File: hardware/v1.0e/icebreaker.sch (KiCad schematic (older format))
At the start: 133 parts, among them J1 Jumper, J10 Jumper, J11 Jumper, J12 Jumper, J13 Jumper, J14 Jumper, J15 Jumper, J16 Jumper, J17 Jumper, J18 Jumper, J19 Jumper, J2 Jumper, J20 Flash, J21 PMOD, J22 PMOD, J23 PMOD, J24 PMOD, J25 RGB Led, J26 5V AUX, J27 5V AUX, J28 CRESET, J29 Jumper, J3 Jumper, J30 Jumper, J31 RGB Led, J32 WS2812, J33 RGB Led, J34 SADD, J4 Jumper, J5 Jumper, J6 Jumper, J7 Jumper, J8 Jumper, J9 Jumper, P1 pkl_USB_OTG, P2 UP, P3 UP, P4 UP, P5 UP, P6 RAM_CS, Q1 BSS138, SW1 TACT, SW2 TACT, SW3 TACT, SW4 TACT, U1 93C46B-SOT-23-6, U2 3.3V, U3 1V2, U4 FT2232H, U5 W25Q, U6 ICE5LP4K-SG48, U7 12MHz

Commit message: Corrected the RGB pin numbering.
The original symbol was based on the older ice5lp not ice40up. The
numbering/naming of those pins changed. Now it should be fixed.

Fixes #31 and #32
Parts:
- U6: value ICE5LP4K-SG48 -> ICE40UP5K-SG48; symbol pkl_lattice:ICE5LP4K-SG48 -> pkl_lattice:ICE40UP5K-SG48
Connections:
- net EB_OD0: now also J33.2 (Pin_2), J34.2 (Pin_2), R28.1; no longer J33.4 (Pin_4)
- net EB_OD2: now also J33.4 (Pin_4); no longer J33.2 (Pin_2), J34.2 (Pin_2), R28.1
- net ET_OD0: now also J31.2 (Pin_2), Q1.1 (G), R7.2; no longer J31.4 (Pin_4)
- net ET_OD2: now also J31.4 (Pin_4); no longer J31.2 (Pin_2), Q1.1 (G), R7.2
- net ~LED_RGB0: now also D11.1 (RK), J25.2 (Pin_2), U6.39 (RGB0); no longer D11.3 (BK), J25.4 (Pin_4), U6.41 (RGB0)
- net ~LED_RGB2: now also D11.3 (BK), J25.4 (Pin_4), U6.41 (RGB2); no longer D11.1 (RK), J25.2 (Pin_2), U6.39 (RGB2)
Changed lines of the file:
@@
 Title "iCEBreaker"
 Date ""
-Rev "V1.0d"
+Rev "V1.0e"
 Comp "1BitSquared"
 Comment1 "2019 (C) 1BitSquared <info@1bitsquared.com>"
@@
 $EndDescr
 $Comp
-L pkl_lattice:ICE5LP4K-SG48 U6
+L pkl_lattice:ICE40UP5K-SG48 U6
 U 1 1 5A512943
 P 9600 4200
 F 0 "U6" H 9600 6370 50  0000 C CNN
-F 1 "ICE5LP4K-SG48" H 9600 6277 50  0000 C CNN
+F 1 "ICE40UP5K-SG48" H 9600 6277 50  0000 C CNN
 F 2 "pkl_housings_dfn_qfn:QFN-48-1EP_7x7mm_Pitch0.5mm" H 11900 4400 50  0001 C CNN
 F 3 "" H 11900 4400 50  0001 C CNN
@@
 	10600 4100 10800 4100
 Text Label 10800 4100 0    50   ~ 0
-~LED_RGB0
+~LED_RGB2
 Text Label 10800 4000 0    50   ~ 0
 ~LED_RGB1
 Text Label 10800 3900 0    50   ~ 0
-~LED_RGB2
+~LED_RGB0
 Text Notes 600  1700 0    100  ~ 0
 FTDI Programmer/UART/FIFO
@@
 ~LED_RGB1
 Text Label 15600 8600 0    50   ~ 0
-~LED_RGB2
-Text Label 15600 8700 0    50   ~ 0
 ~LED_RGB0
+Text Label 15600 8700 0    50   ~ 0
+~LED_RGB2
 Wire Wire Line
 	13300 4400 13500 4400
@@
 	15150 9700 15250 9700
 Text Label 15250 9300 0    50   ~ 0
-~LED_RGB2
+~LED_RGB0
 Text Label 15250 9500 0    50   ~ 0
 ~LED_RGB1
 Text Label 15250 9700 0    50   ~ 0
-~LED_RGB0
+~LED_RGB2
 $Comp
 L pkl_misc:pkl_double_jumper_ncno J30
@@
 	7400 10400 7300 10400
 Text Label 8000 10400 0    50   ~ 0
-ET_OD2
-Text Label 7300 10400 2    50   ~ 0
-ET_OD1
-Text Label 8000 10500 0    50   ~ 0
 ET_OD0
+Text Label 8000 10500 0    50   ~ 0
+ET_OD2
 Wire Wire Line
 	7300 10600 7400 10600
@@
 Connection ~ 8700 10800
 Text Label 8600 10800 2    50   ~ 0
-ET_OD2
+ET_OD0
 Wire Wire Line
 	8600 10300 8700 10300
@@
 	9900 10400 9800 10400
 Text Label 10500 10400 0    50   ~ 0
-EB_OD2
+EB_OD0
 Text Label 9800 10400 2    50   ~ 0
 EB_OD1
 Text Label 10500 10500 0    50   ~ 0
-EB_OD0
+EB_OD2
 Wire Wire Line
 	9800 10600 9900 10600
@@
 Connection ~ 11300 11000
 Text Label 11400 10900 0    50   ~ 0
-EB_OD2
+EB_OD0
 Text Label 11400 11000 0    50   ~ 0
 EB_OD1
@@
 Text Notes 550  5500 0    50   ~ 0
 We need the FTDI flash.\nWe program a unique serial\nso multiple iCEBreakers can\nbe used at the same time.
+Text Label 7300 10400 2    50   ~ 0
+ET_OD1
 $EndSCHEMATC

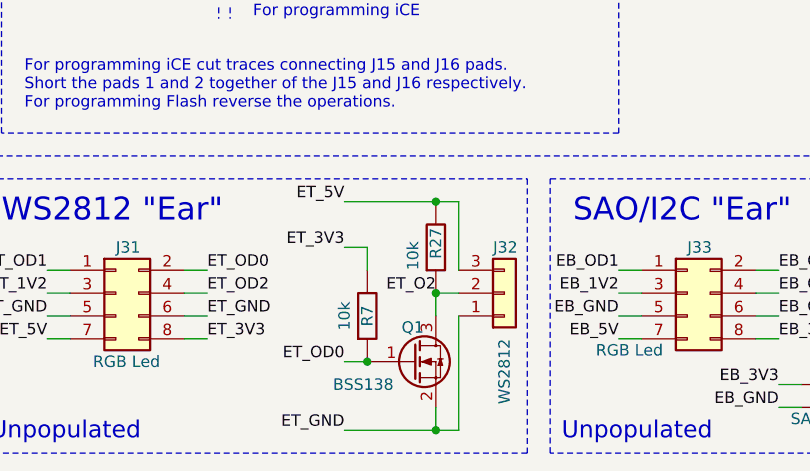
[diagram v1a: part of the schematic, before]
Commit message: Corrected one of the ear net names to match the RGB led net changes.
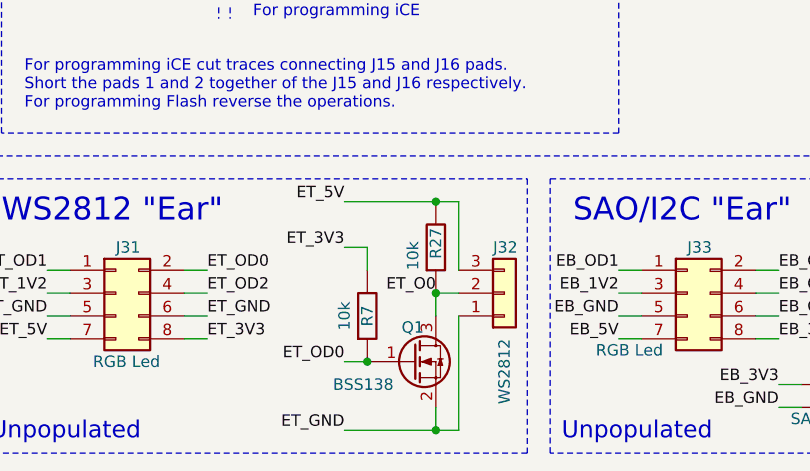
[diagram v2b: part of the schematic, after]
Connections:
- net ET_O2 renamed ET_O0
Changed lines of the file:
@@
 Connection ~ 9000 11100
 Text Label 9000 10500 2    50   ~ 0
-ET_O2
+ET_O0
 $Comp
 L Connector_Generic:Conn_02x04_Odd_Even J33

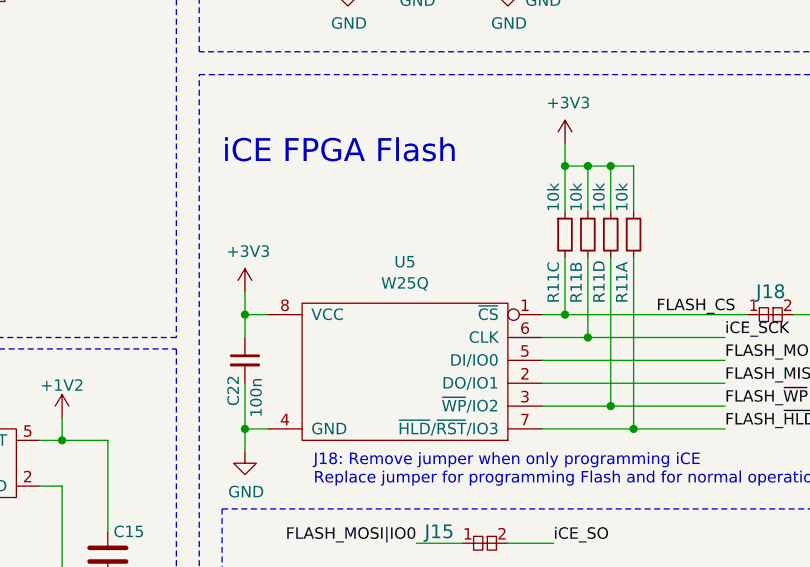
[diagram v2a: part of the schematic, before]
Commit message: Added exact FPGA EEPROM type and datasheet link.
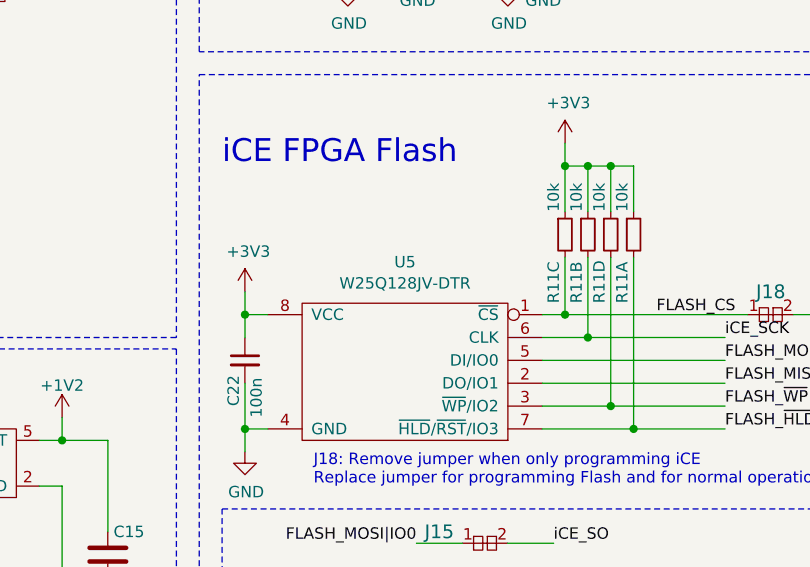
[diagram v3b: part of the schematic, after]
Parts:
- U5: value W25Q -> W25Q128JV-DTR; MFN (none) -> W25Q128JVSIM
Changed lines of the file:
@@
 P 7900 7950
 F 0 "U5" H 7900 8380 50  0000 C CNN
-F 1 "W25Q" H 7900 8287 50  0000 C CNN
+F 1 "W25Q128JV-DTR" H 7900 8287 50  0000 C CNN
 F 2 "pkl_housings_soic:SOIC-8_5.3x5.3mm_Pitch1.27mm" H 7900 7950 50  0001 C CNN
-F 3 "" H 7900 7950 50  0001 C CNN
+F 3 "https://www.winbond.com/resource-files/w25q128jv%20dtr%20revb%2011042016.pdf" H 7900 7950 50  0001 C CNN
 F 4 "ANY" H 7900 7950 50  0001 C CNN "Source"
 F 5 "eeprom-so8w-W25Q" H 0   0   50  0001 C CNN "Key"
+F 6 "W25Q128JVSIM" H 7900 7950 50  0001 C CNN "MFN"
 	1    7900 7950
 	-1   0    0    -1
